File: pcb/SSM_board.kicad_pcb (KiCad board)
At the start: 4 copper layers, 100 x 100 mm, 184 parts, among them IC1 STPIC6C595TTR, IC2 STPIC6C595TTR, IC3 STPIC6C595TTR, IC4 STPIC6C595TTR, IC5 STPIC6C595TTR, IC6 STPIC6C595TTR, IC7 STPIC6C595TTR, IC8 STPIC6C595TTR, J1 DA15_Pins_MountingHoles, J2 DA15_Pins_MountingHoles, U101 GAQY212GS, U102 GAQY212GS, U103 GAQY212GS, U104 GAQY212GS, U105 GAQY212GS, U106 GAQY212GS, U107 GAQY212GS, U108 GAQY212GS, U201 GAQY212GS, U202 GAQY212GS, U203 GAQY212GS, U204 GAQY212GS, U205 GAQY212GS, U206 GAQY212GS, U207 GAQY212GS, U208 GAQY212GS, U301 GAQY212GS, U302 GAQY212GS, U303 GAQY212GS, U304 GAQY212GS, U305 GAQY212GS, U306 GAQY212GS, U307 GAQY212GS, U308 GAQY212GS, U401 GAQY212GS, U402 GAQY212GS, U403 GAQY212GS, U404 GAQY212GS, U405 GAQY212GS, U406 GAQY212GS, U407 GAQY212GS, U408 GAQY212GS, U501 GAQY212GS, U502 GAQY212GS, U503 GAQY212GS, U504 GAQY212GS, U505 GAQY212GS, U506 GAQY212GS, U507 GAQY212GS, U508 GAQY212GS, U601 GAQY212GS, U602 GAQY212GS, U603 GAQY212GS, U604 GAQY212GS, U605 GAQY212GS, U606 GAQY212GS, U607 GAQY212GS, U608 GAQY212GS, U609 GAQY212GS, U610 GAQY212GS, U611 GAQY212GS, U612 GAQY212GS, U701 GAQY212GS, U702 GAQY212GS, U703 GAQY212GS, U704 GAQY212GS, U705 GAQY212GS, U706 GAQY212GS, U707 GAQY212GS, U708 GAQY212GS, U709 GAQY212GS, U710 GAQY212GS, U711 GAQY212GS, U712 GAQY212GS

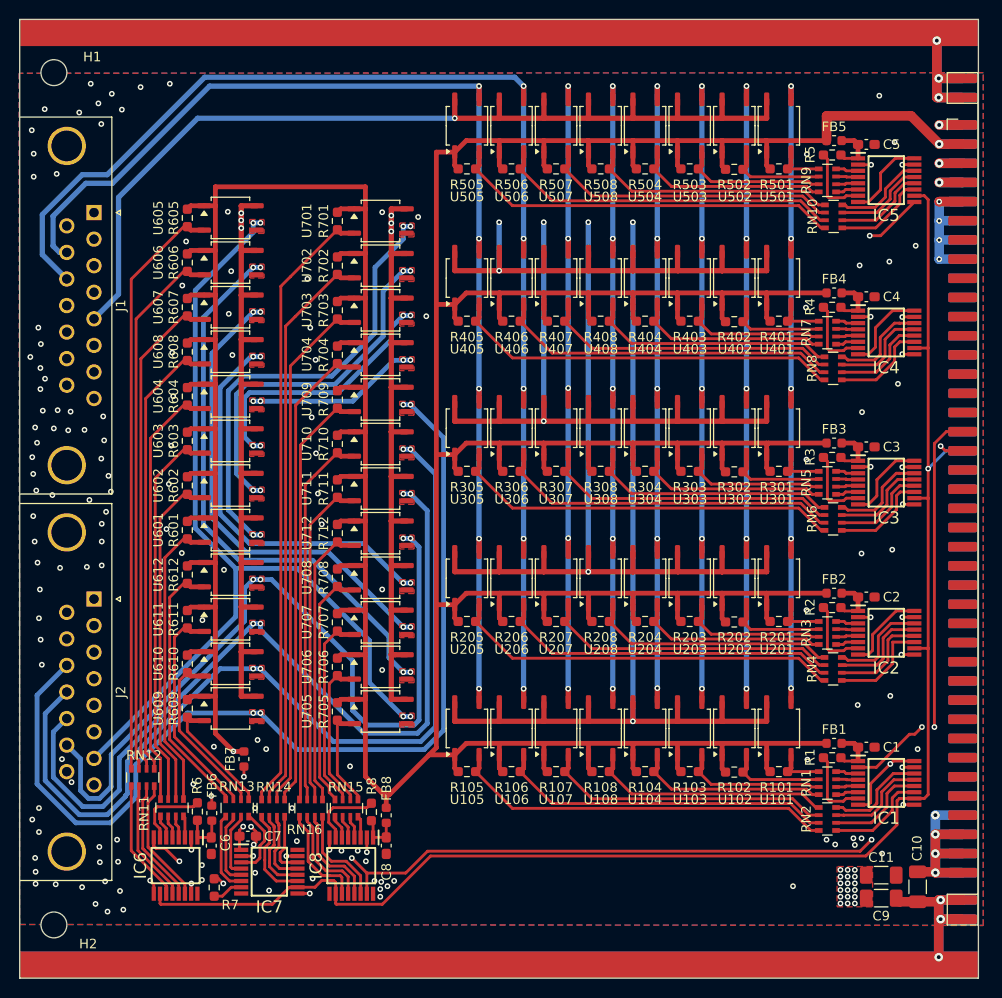
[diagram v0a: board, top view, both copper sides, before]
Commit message: Added vias
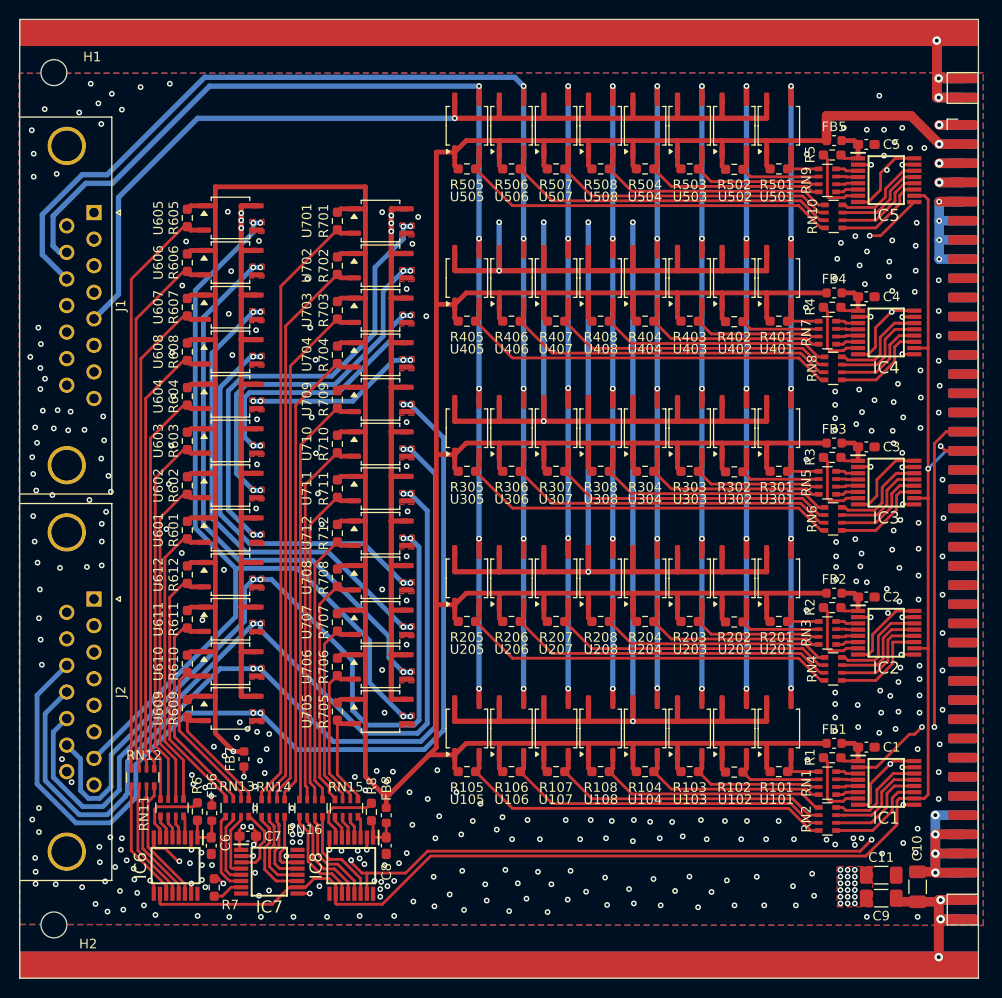
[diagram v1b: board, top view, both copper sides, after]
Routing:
- net /Conn/SSR_SCK: track 168.7 -> 169.5 mm
- net GND: vias 75 -> 275
- net Earth_Protective: vias 97 -> 114
